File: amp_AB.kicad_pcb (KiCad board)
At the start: 2 copper layers, 95 x 45 mm, 19 parts, among them J1 Power, J2 Audio, J3 Conn_01x02, J4 Pot_10k, Q1 TIP141, Q2 TIP146, U2 NE5532

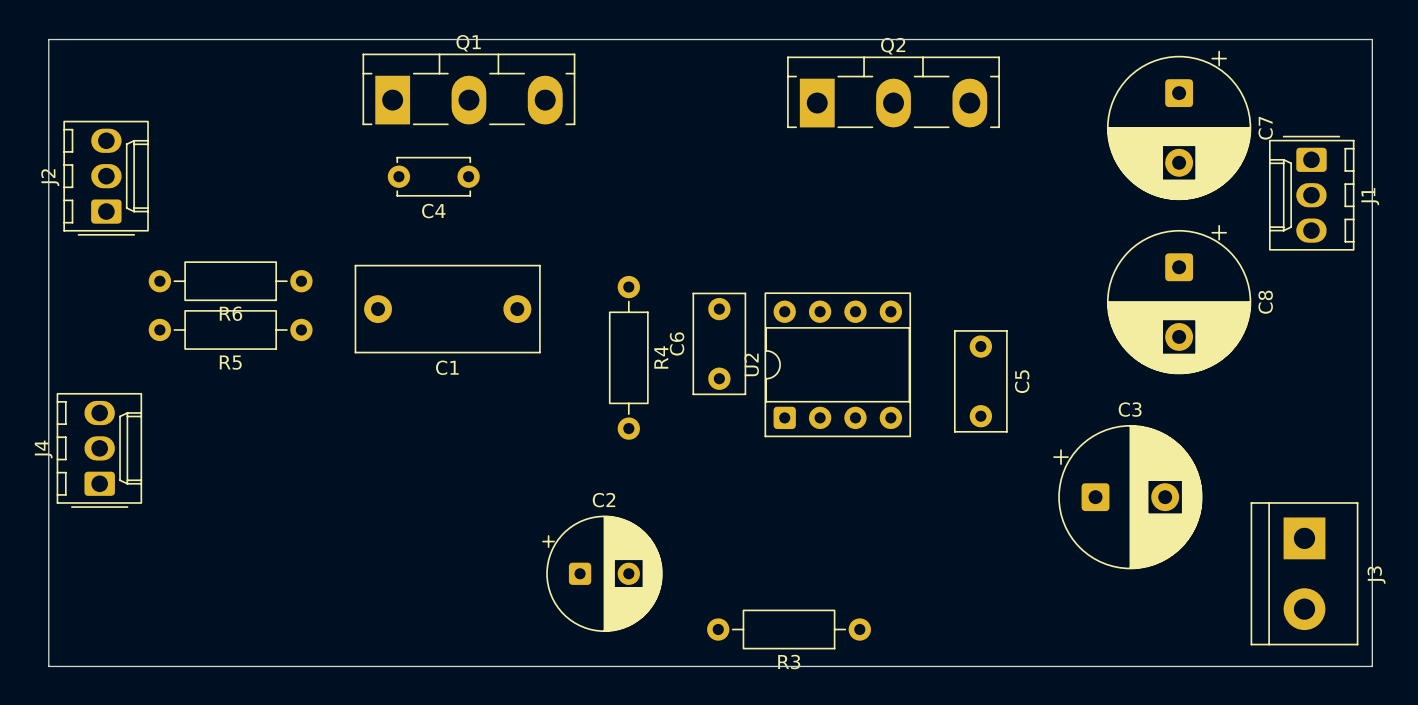
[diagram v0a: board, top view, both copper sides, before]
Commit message: Termine el routing y puse los mounting holes
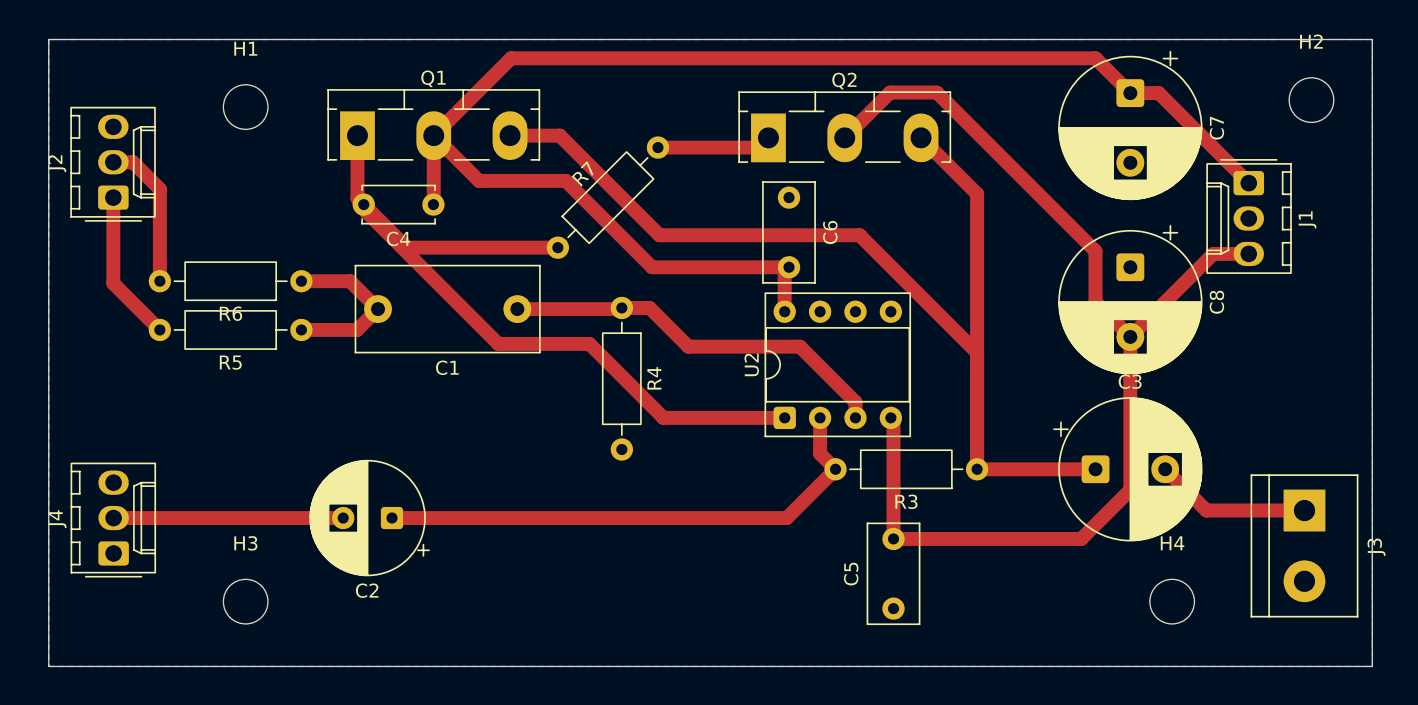
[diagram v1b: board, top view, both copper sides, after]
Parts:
- added H1: MountingHole, MountingHole:MountingHole_3.2mm_M3, F.Cu at (113.0, 74.5)
- added H2: MountingHole, MountingHole:MountingHole_3.2mm_M3, F.Cu at (189.5, 74.0)
- added H3: MountingHole, MountingHole:MountingHole_3.2mm_M3, F.Cu at (113.0, 110.0)
- added H4: MountingHole, MountingHole:MountingHole_3.2mm_M3, F.Cu at (179.5, 110.0)
- added R7: 0, Resistor_THT:R_Axial_DIN0207_L6.3mm_D2.5mm_P10.16mm_Horizontal, F.Cu at (135.4, 84.6)
- moved C5 19.8 mm to (159.5, 110.5), turned to 90 degrees
- moved R3 14.3 mm to (165.5, 100.5)
- moved C2 14.1 mm to (123.5, 104.0), turned to 180 degrees
- moved C6 13.9 mm to (152.0, 81.0), turned to -90 degrees
- moved J4 5.10 mm to (103.5, 106.5)
- moved J1 4.80 mm to (185.0, 80.0)
- moved Q2 4.30 mm to (150.5, 76.7)
- moved Q1 3.59 mm to (121.0, 76.5)
- moved C7 3.50 mm to (176.5, 73.5)
- moved C8 3.50 mm to (176.5, 86.0)
- moved C4 3.22 mm to (126.5, 81.5)
- moved C3 2.00 mm to (174.0, 100.5)
- moved J3 2.00 mm to (189.0, 103.5)
- moved R4 1.58 mm to (140.0, 88.9)
- moved J2 1.12 mm to (103.5, 81.0)
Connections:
- Q2 pad 1: Net-(Q1-B) -> Net-(Q2-B)
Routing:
- net VCC: track 0.00 -> 102.5 mm
- net Net-(C3-A): track 0.00 -> 82.3 mm
- net VEE: track 0.00 -> 80.4 mm
- net Net-(Q1-B): track 0.00 -> 57.7 mm
- net Net-(C2-A): track 0.00 -> 37.4 mm
- net Net-(U2A-+): track 0.00 -> 28.2 mm
- net Net-(C2-B): track 0.00 -> 16.5 mm
- net Net-(C1-Pad2): track 0.00 -> 12.4 mm
- net Net-(C3-B): track 0.00 -> 11.2 mm
- net /L: track 0.00 -> 10.9 mm
- net /R: track 0.00 -> 10.7 mm
- net Net-(Q2-B): track 0.00 -> 8.22 mm
- added copper zone on B.Cu, net GND

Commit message: listo el pollo falta la carcasa
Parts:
- moved R3 1.00 mm to (165.5, 101.5)
- moved H2 0.50 mm to (189.5, 74.5)
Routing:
- net Net-(C3-A): track 82.3 -> 86.2 mm
- net VEE: track 80.4 -> 81.6 mm
- net /R: track 10.7 -> 11.5 mm
- net /L: track 10.9 -> 11.5 mm
- net Net-(Q1-B): track 57.7 -> 58.3 mm
- net Net-(C2-A): track 37.4 -> 38.0 mm
- added copper zone on F.Cu, net GND
- removed copper zone on B.Cu, net GND

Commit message: Ultimos detalles y exportado de gerbers
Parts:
- moved H1 10.2 mm to (102.8, 73.7)
- moved J2 9.13 mm to (102.8, 90.1)
- moved Q1 4.70 mm to (116.3, 76.5)
- moved C4 4.70 mm to (121.8, 81.5)
- moved R5 1.08 mm to (118.1, 90.5)
- moved R6 1.08 mm to (118.1, 87.0)
- moved H2 0.94 mm to (189.9, 73.7)
- moved J4 0.70 mm to (102.8, 106.5)
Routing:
- net VCC: track 102.5 -> 111.5 mm
- net /L: track 11.5 -> 5.29 mm
- net /R: track 11.5 -> 5.35 mm
- net Net-(C3-A): track 86.2 -> 90.9 mm
- net Net-(Q1-B): track 58.3 -> 60.6 mm
- net Net-(C1-Pad2): track 12.4 -> 10.3 mm
- net Net-(C2-B): track 16.5 -> 17.2 mm
- added copper zone on B.Cu, net GND
- removed copper zone on F.Cu, net GND

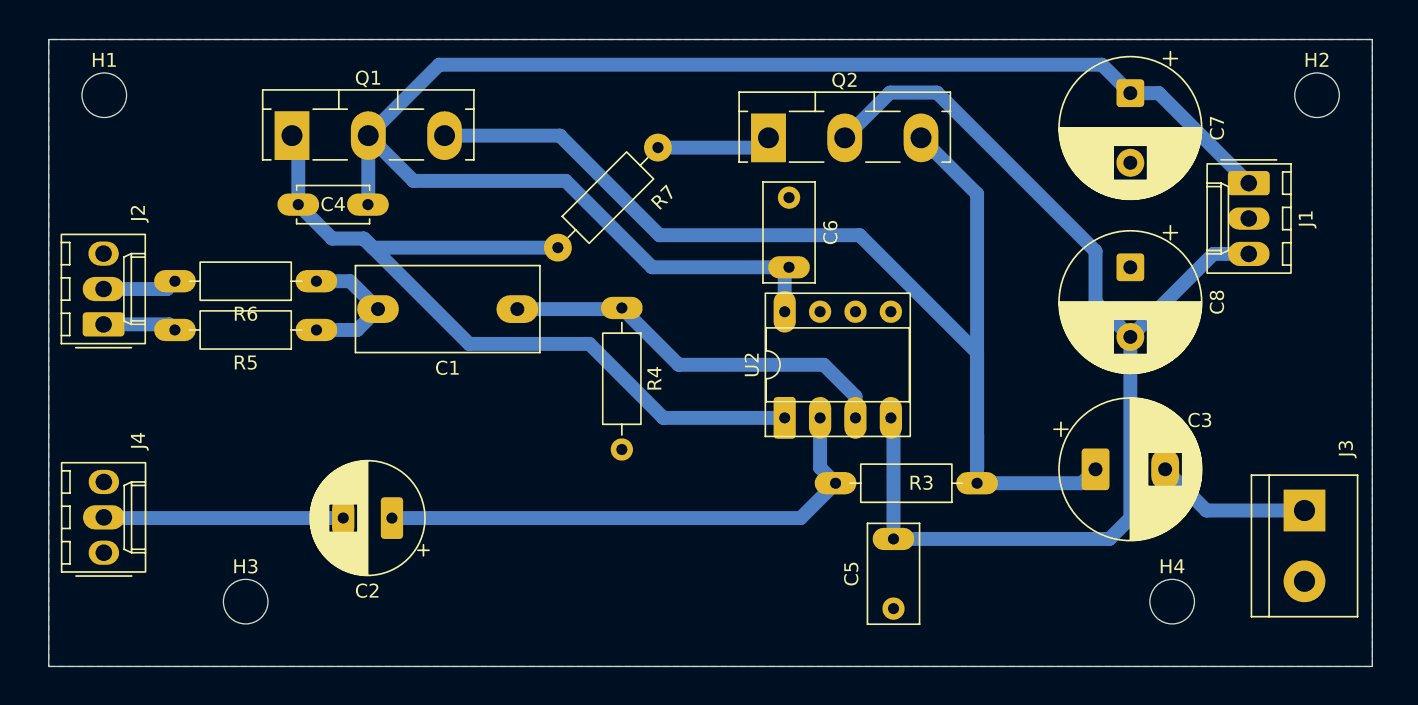
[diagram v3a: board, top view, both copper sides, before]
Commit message: Corregidas las islas desconectadas
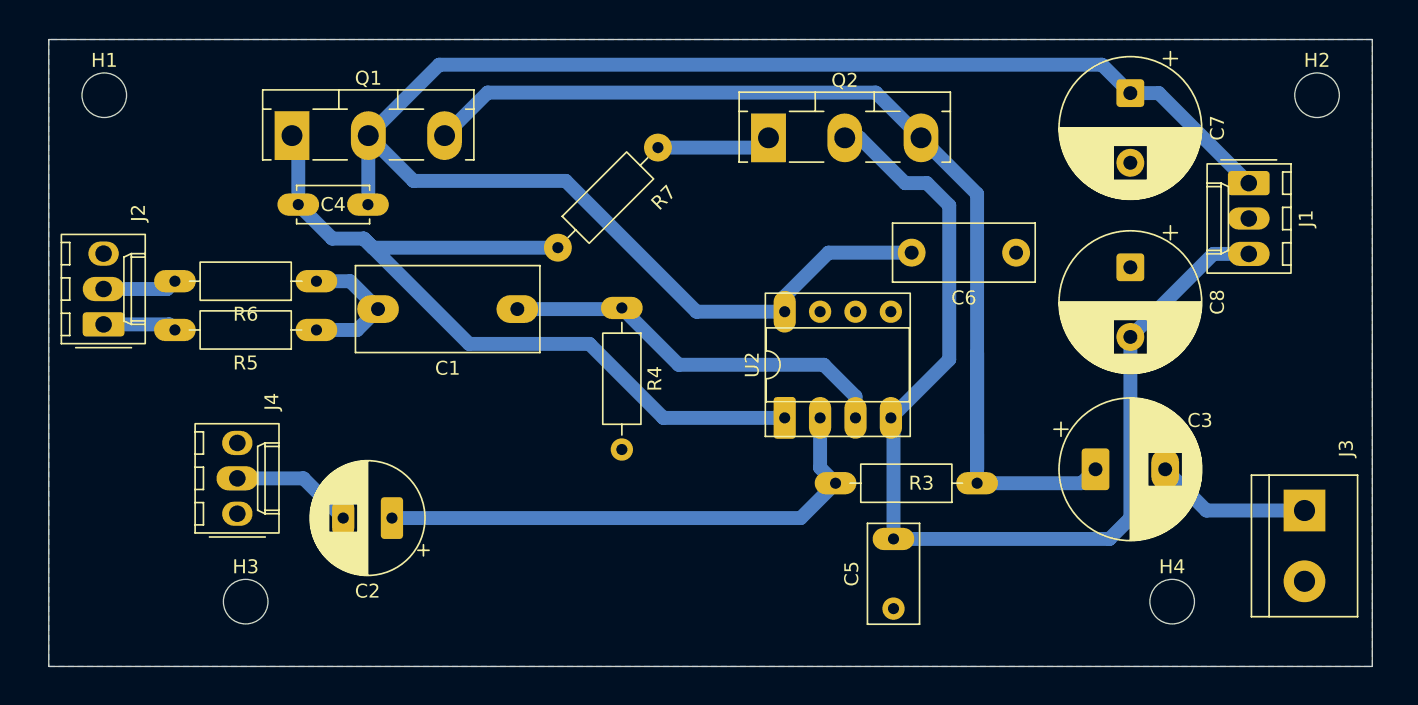
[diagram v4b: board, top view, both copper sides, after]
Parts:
- C6: footprint Capacitor_THT:C_Rect_L7.0mm_W3.5mm_P5.00mm -> Capacitor_THT:C_Rect_L10.0mm_W4.0mm_P7.50mm_MKS4
- moved C6 16.8 mm to (168.3, 85.0), turned to 180 degrees
- moved J4 9.98 mm to (112.4, 103.7)
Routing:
- net VCC: track 111.5 -> 120.7 mm
- net Net-(C2-B): track 17.2 -> 8.85 mm
- net Net-(C3-A): track 90.9 -> 83.1 mm
- net VEE: track 81.6 -> 76.9 mm
